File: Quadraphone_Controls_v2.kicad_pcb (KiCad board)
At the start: 2 copper layers, 60 x 110 mm, 26 parts, among them J1 Conn_01x10_Female, J10 Pitch_In, J11 Mix_Out, J12 Conn_02x04_Odd_Even, J13 Conn_01x04_Male, J14 Conn_01x01_Male, J2 Conn_01x10_Female, J3 Conn_01x10_Female, J4 Conn_01x10_Female, J5 PWM_CV, J6 LFO_IN, J7 PWM_CV_In, J8 Synch_Signal_In, J9 Freq_Mod_In, SW1 Synch_Type, SW2 Output_Type, SW3 Output_Type

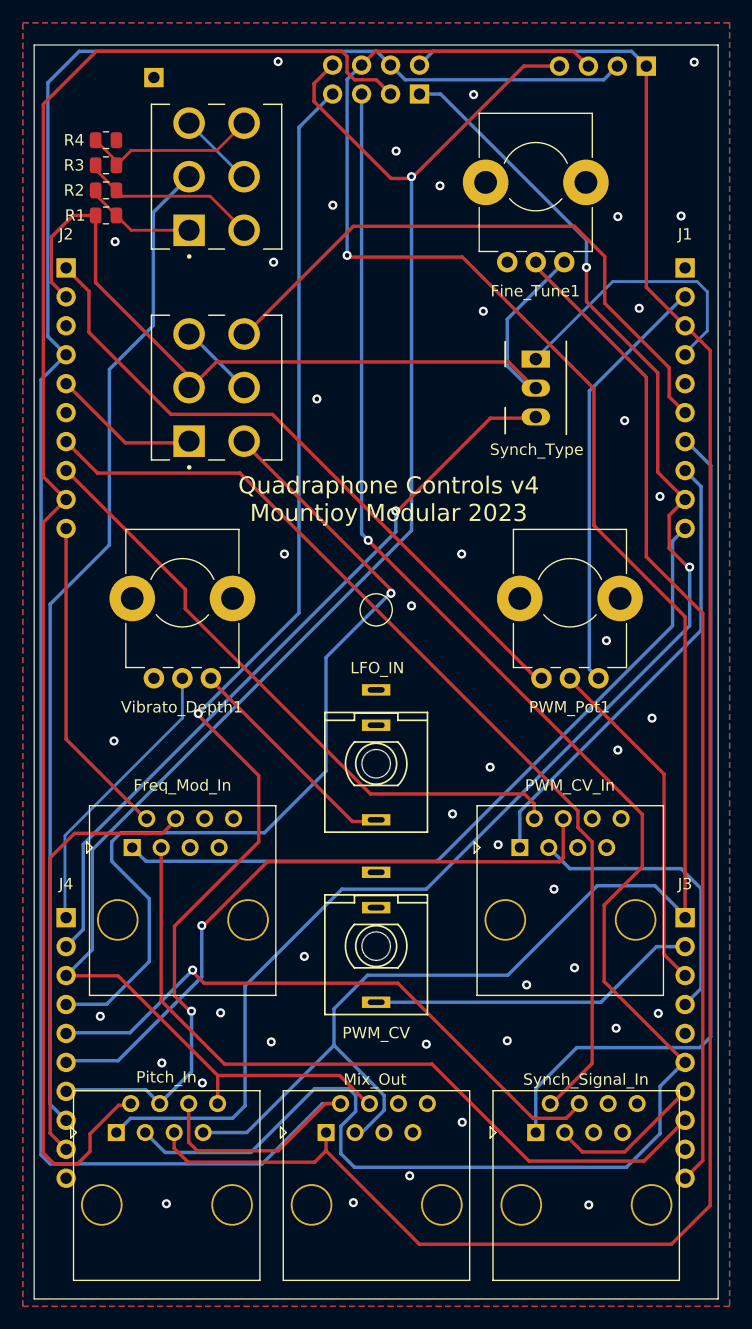
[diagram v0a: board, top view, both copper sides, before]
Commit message: Create gerbers for control board changes;
Notes for potential v3 component revision
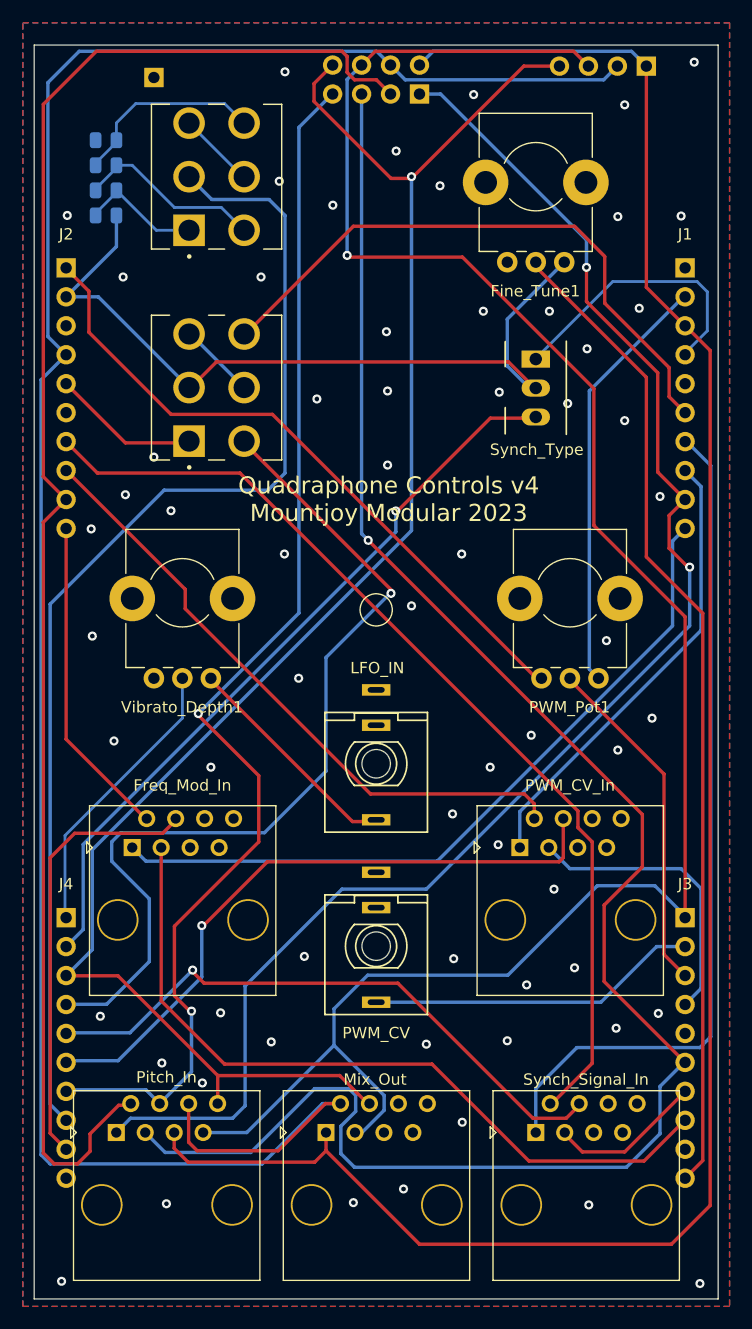
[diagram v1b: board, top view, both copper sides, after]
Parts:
- R1, R2, R3, R4: moved to B.Cu
- turned R1 to 180 degrees
- turned R2 to 180 degrees
- turned R3 to 180 degrees
- turned R4 to 180 degrees
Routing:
- net /OCT_TUNE: track 88.4 -> 103.6 mm
- net +5V: track 75.8 -> 69.9 mm
- net /Oct_2v: track 15.7 -> 17.1 mm
- net /Oct_3v: track 15.6 -> 16.5 mm
- net /Oct_4v: track 9.87 -> 10.8 mm
- net GND: vias 43 -> 64
